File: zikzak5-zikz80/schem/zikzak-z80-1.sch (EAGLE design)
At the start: 65 parts, among them IC1 Z80, IC10 74LS32N, IC11 74LS32N, IC12 74LS32N, IC13 74LS32N, IC14 74LS04N, IC15 74LS32N, IC2 ATMEGA644-20PU, IC3 MC6850, IC4 74LS32N, IC5 74LS04N, IC6 74LS32N, IC7 74LS04N, IC8 74LS04N, IC9 74LS04N, U2 FT232RLSSOP, X2 USB-SMD-NS

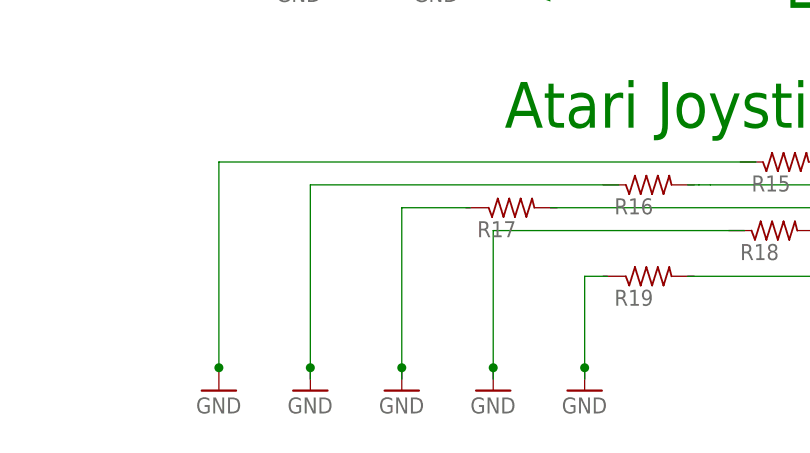
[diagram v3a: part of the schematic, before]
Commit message: basic joystick sensing.. works! corrections to schematic (pull up, not down, on joystick.)
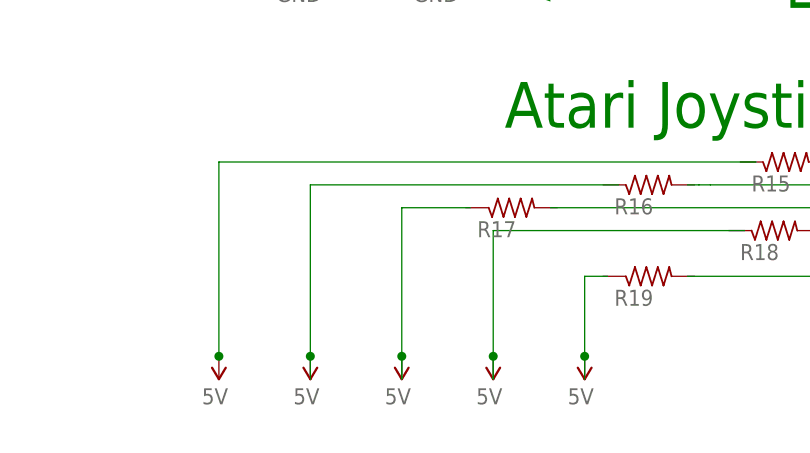
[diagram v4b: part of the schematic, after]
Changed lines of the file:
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@@
 <setting verticaltext="up"/>
 </settings>
-<grid distance="0.05" unitdist="inch" unit="inch" style="dots" multiple="1" display="yes" altdistance="0.01" altunitdist="inch" altunit="inch"/>
+<grid distance="0.1" unitdist="inch" unit="inch" style="lines" multiple="1" display="no" altdistance="0.01" altunitdist="inch" altunit="inch"/>
 <layers>
 <layer number="1" name="Top" color="4" fill="1" visible="no" active="no"/>
@@
 <part name="R18" library="rcl" deviceset="R-US_" device="0204/2V"/>
 <part name="R19" library="rcl" deviceset="R-US_" device="0204/2V"/>
-<part name="GND14" library="SparkFun" deviceset="GND" device=""/>
-<part name="GND15" library="SparkFun" deviceset="GND" device=""/>
-<part name="GND16" library="SparkFun" deviceset="GND" device=""/>
-<part name="GND17" library="SparkFun" deviceset="GND" device=""/>
-<part name="GND18" library="SparkFun" deviceset="GND" device=""/>
 <part name="U$13" library="adafruit" deviceset="PS603" device="SPK"/>
 <part name="GND19" library="SparkFun" deviceset="GND" device=""/>
 <part name="GND20" library="SparkFun" deviceset="GND" device=""/>
+<part name="U$2" library="SparkFun" deviceset="5V" device=""/>
+<part name="U$15" library="SparkFun" deviceset="5V" device=""/>
+<part name="U$16" library="SparkFun" deviceset="5V" device=""/>
+<part name="U$17" library="SparkFun" deviceset="5V" device=""/>
+<part name="U$18" library="SparkFun" deviceset="5V" device=""/>
 </parts>
 <sheets>
@@
 <instance part="R18" gate="G$1" x="414.782" y="26.67" rot="MR180"/>
 <instance part="R19" gate="G$1" x="400.812" y="21.59" rot="MR180"/>
-<instance part="GND14" gate="1" x="393.7" y="8.89"/>
-<instance part="GND15" gate="1" x="383.54" y="8.89"/>
-<instance part="GND16" gate="1" x="373.38" y="8.89"/>
-<instance part="GND17" gate="1" x="363.22" y="8.89"/>
-<instance part="GND18" gate="1" x="353.06" y="8.89"/>
 <instance part="U$13" gate="G$1" x="435.61" y="69.85" rot="R180"/>
 <instance part="GND19" gate="1" x="444.5" y="58.42"/>
 <instance part="GND20" gate="1" x="369.57" y="187.96" rot="R180"/>
+<instance part="U$2" gate="G$1" x="353.06" y="12.7" rot="R180"/>
+<instance part="U$15" gate="G$1" x="363.22" y="12.7" rot="R180"/>
+<instance part="U$16" gate="G$1" x="373.38" y="12.7" rot="R180"/>
+<instance part="U$17" gate="G$1" x="383.54" y="12.7" rot="R180"/>
+<instance part="U$18" gate="G$1" x="393.7" y="12.7" rot="R180"/>
 </instances>
 <busses>
@@
 <junction x="434.34" y="10.16"/>
 <wire x1="434.34" y1="10.16" x2="434.34" y2="8.89" width="0.1524" layer="91"/>
-</segment>
-<segment>
-<pinref part="GND18" gate="1" pin="GND"/>
-<wire x1="412.75" y1="34.29" x2="353.06" y2="34.29" width="0.1524" layer="91"/>
-<wire x1="353.06" y1="34.29" x2="353.06" y2="11.43" width="0.1524" layer="91"/>
-<junction x="353.06" y="11.43"/>
-</segment>
-<segment>
-<wire x1="397.51" y1="31.75" x2="363.22" y2="31.75" width="0.1524" layer="91"/>
-<wire x1="363.22" y1="31.75" x2="363.22" y2="11.43" width="0.1524" layer="91"/>
-<pinref part="GND17" gate="1" pin="GND"/>
-<junction x="363.22" y="11.43"/>
-<wire x1="363.22" y1="11.43" x2="363.22" y2="10.16" width="0.1524" layer="91"/>
-</segment>
-<segment>
-<wire x1="381" y1="29.21" x2="373.38" y2="29.21" width="0.1524" layer="91"/>
-<wire x1="373.38" y1="29.21" x2="373.38" y2="11.43" width="0.1524" layer="91"/>
-<pinref part="GND16" gate="1" pin="GND"/>
-<junction x="373.38" y="11.43"/>
-<wire x1="373.38" y1="11.43" x2="373.38" y2="10.16" width="0.1524" layer="91"/>
-</segment>
-<segment>
-<wire x1="411.48" y1="26.67" x2="383.54" y2="26.67" width="0.1524" layer="91"/>
-<wire x1="383.54" y1="26.67" x2="383.54" y2="11.43" width="0.1524" layer="91"/>
-<pinref part="GND15" gate="1" pin="GND"/>
-<junction x="383.54" y="11.43"/>
-<wire x1="383.54" y1="11.43" x2="383.54" y2="10.16" width="0.1524" layer="91"/>
-</segment>
-<segment>
-<wire x1="396.24" y1="21.59" x2="393.7" y2="21.59" width="0.1524" layer="91"/>
-<wire x1="393.7" y1="21.59" x2="393.7" y2="11.43" width="0.1524" layer="91"/>
-<pinref part="GND14" gate="1" pin="GND"/>
-<junction x="393.7" y="11.43"/>
-<wire x1="393.7" y1="11.43" x2="393.7" y2="10.16" width="0.1524" layer="91"/>
 </segment>
 <segment>
@@
 <label x="452.12" y="127" size="1.27" layer="95" xref="yes"/>
 </segment>
+<segment>
+<wire x1="412.75" y1="34.29" x2="353.06" y2="34.29" width="0.1524" layer="91"/>
+<wire x1="353.06" y1="34.29" x2="353.06" y2="12.7" width="0.1524" layer="91"/>
+<pinref part="U$2" gate="G$1" pin="5V"/>
+<junction x="353.06" y="12.7"/>
+</segment>
+<segment>
+<wire x1="397.51" y1="31.75" x2="363.22" y2="31.75" width="0.1524" layer="91"/>
+<wire x1="363.22" y1="31.75" x2="363.22" y2="12.7" width="0.1524" layer="91"/>
+<pinref part="U$15" gate="G$1" pin="5V"/>
+<wire x1="363.22" y1="12.7" x2="363.22" y2="10.16" width="0.1524" layer="91"/>
+<junction x="363.22" y="12.7"/>
+</segment>
+<segment>
+<wire x1="381" y1="29.21" x2="373.38" y2="29.21" width="0.1524" layer="91"/>
+<wire x1="373.38" y1="29.21" x2="373.38" y2="12.7" width="0.1524" layer="91"/>
+<pinref part="U$16" gate="G$1" pin="5V"/>
+<wire x1="373.38" y1="12.7" x2="373.38" y2="10.16" width="0.1524" layer="91"/>
+<junction x="373.38" y="12.7"/>
+</segment>
+<segment>
+<wire x1="411.48" y1="26.67" x2="383.54" y2="26.67" width="0.1524" layer="91"/>
+<wire x1="383.54" y1="26.67" x2="383.54" y2="12.7" width="0.1524" layer="91"/>
+<pinref part="U$17" gate="G$1" pin="5V"/>
+<wire x1="383.54" y1="12.7" x2="383.54" y2="10.16" width="0.1524" layer="91"/>
+<junction x="383.54" y="12.7"/>
+</segment>
+<segment>
+<wire x1="396.24" y1="21.59" x2="393.7" y2="21.59" width="0.1524" layer="91"/>
+<wire x1="393.7" y1="21.59" x2="393.7" y2="12.7" width="0.1524" layer="91"/>
+<pinref part="U$18" gate="G$1" pin="5V"/>
+<wire x1="393.7" y1="12.7" x2="393.7" y2="10.16" width="0.1524" layer="91"/>
+<junction x="393.7" y="12.7"/>
+</segment>
 </net>
